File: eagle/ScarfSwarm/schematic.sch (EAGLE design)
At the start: 5 parts

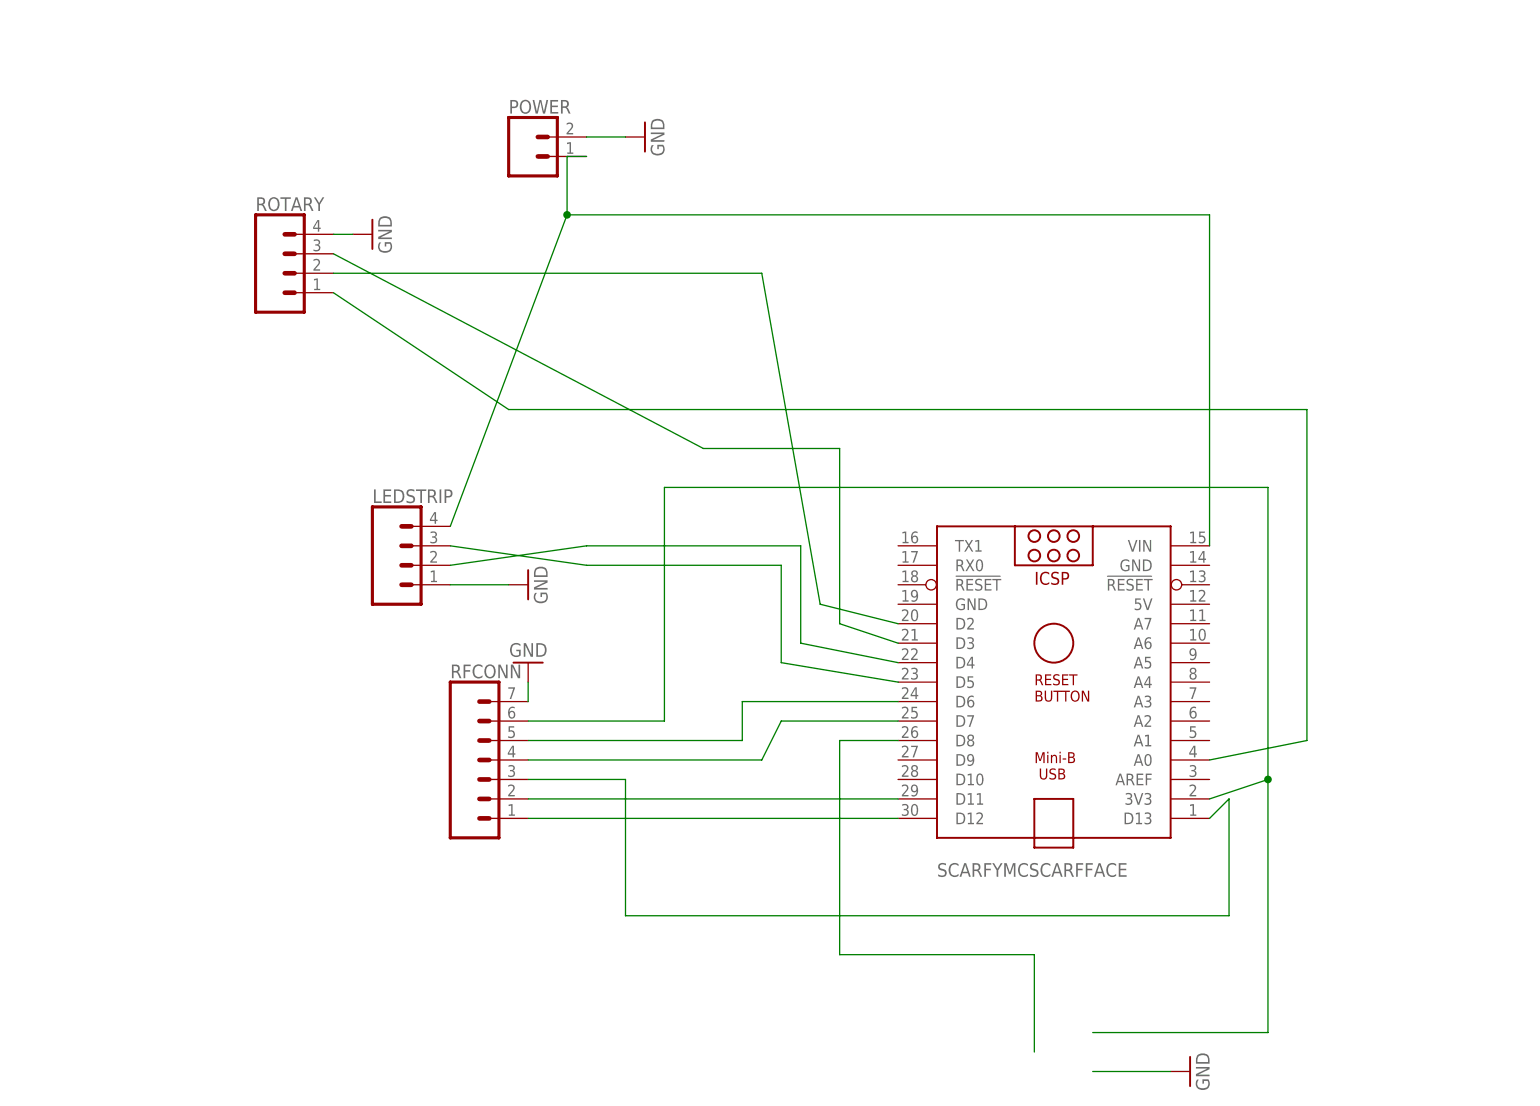
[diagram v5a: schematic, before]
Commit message: reorder radio contacts so that they are easy to solder
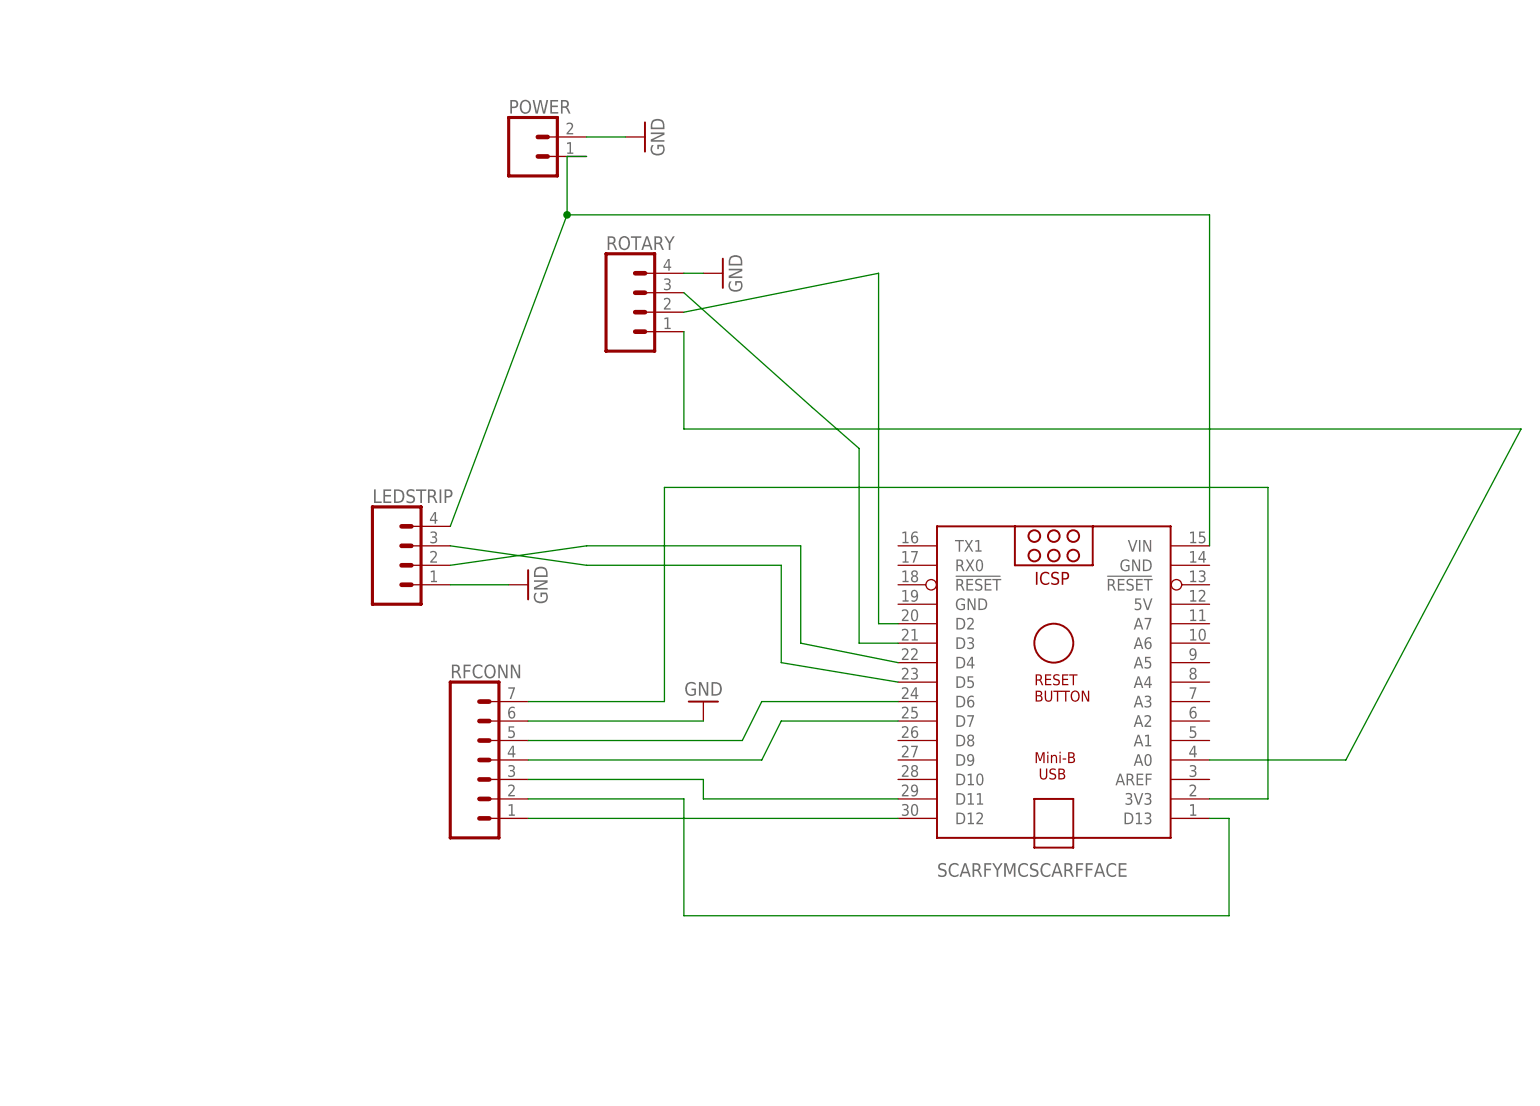
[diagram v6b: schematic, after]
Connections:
- removed net N$7 (its old number): SCARFYMCSCARFFACE.D8
- net GND: now also RFCONN.6; no longer RFCONN.7
- net N$1: now also RFCONN.7; no longer RFCONN.6
- net N$4: now also RFCONN.2; no longer RFCONN.3
- net N$5: now also RFCONN.3; no longer RFCONN.2
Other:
- moved on the sheet: ROTARY
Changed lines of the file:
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@@
 <part name="GND2" library="supply1" library_urn="urn:adsk.eagle:library:371" deviceset="GND" device=""/>
 <part name="SCARFYMCSCARFFACE" library="ArduinoNanoV30" deviceset="ARDUINO_NANO" device=""/>
-<part name="GND5" library="supply1" library_urn="urn:adsk.eagle:library:371" deviceset="GND" device=""/>
 </parts>
 <sheets>
@@
 </plain>
 <instances>
-<instance part="GND1" gate="1" x="-7.62" y="76.2" smashed="yes" rot="R90">
-<attribute name="VALUE" x="-5.08" y="73.66" size="1.778" layer="96" rot="R90"/>
+<instance part="GND1" gate="1" x="38.1" y="71.12" smashed="yes" rot="R90">
+<attribute name="VALUE" x="40.64" y="68.58" size="1.778" layer="96" rot="R90"/>
 </instance>
 <instance part="GND3" gate="1" x="12.7" y="30.48" smashed="yes" rot="R90">
 <attribute name="VALUE" x="15.24" y="27.94" size="1.778" layer="96" rot="R90"/>
 </instance>
-<instance part="GND4" gate="1" x="12.7" y="20.32" smashed="yes" rot="R180">
-<attribute name="VALUE" x="15.24" y="22.86" size="1.778" layer="96" rot="R180"/>
+<instance part="GND4" gate="1" x="35.56" y="15.24" smashed="yes" rot="R180">
+<attribute name="VALUE" x="38.1" y="17.78" size="1.778" layer="96" rot="R180"/>
 </instance>
 <instance part="RFCONN" gate="J1" x="7.62" y="5.08" smashed="yes">
@@
 <attribute name="NAME" x="2.54" y="18.288" size="1.778" layer="95" font="vector"/>
 </instance>
-<instance part="ROTARY" gate="J1" x="-17.78" y="71.12" smashed="yes">
-<attribute name="VALUE" x="-22.86" y="63.754" size="1.778" layer="96" font="vector"/>
-<attribute name="NAME" x="-22.86" y="79.248" size="1.778" layer="95" font="vector"/>
+<instance part="ROTARY" gate="J1" x="27.94" y="66.04" smashed="yes">
+<attribute name="VALUE" x="22.86" y="58.674" size="1.778" layer="96" font="vector"/>
+<attribute name="NAME" x="22.86" y="74.168" size="1.778" layer="95" font="vector"/>
 </instance>
 <instance part="LEDSTRIP" gate="J1" x="-2.54" y="33.02" smashed="yes">
@@
 <attribute name="VALUE" x="66.04" y="-10.16" size="1.778" layer="96"/>
 </instance>
-<instance part="GND5" gate="1" x="99.06" y="-33.02" smashed="yes" rot="R90">
-<attribute name="VALUE" x="101.6" y="-35.56" size="1.778" layer="96" rot="R90"/>
-</instance>
 </instances>
 <busses>
@@
 <nets>
 <net name="GND" class="0">
-<segment>
-<pinref part="RFCONN" gate="J1" pin="7"/>
-<pinref part="GND4" gate="1" pin="GND"/>
-<wire x1="12.7" y1="15.24" x2="12.7" y2="17.78" width="0.1524" layer="91"/>
-</segment>
 <segment>
 <pinref part="LEDSTRIP" gate="J1" pin="1"/>
@@
 <pinref part="ROTARY" gate="J1" pin="4"/>
 <pinref part="GND1" gate="1" pin="GND"/>
-<wire x1="-12.7" y1="76.2" x2="-10.16" y2="76.2" width="0.1524" layer="91"/>
+<wire x1="33.02" y1="71.12" x2="35.56" y2="71.12" width="0.1524" layer="91"/>
 </segment>
 <segment>
@@
 </segment>
 <segment>
-<pinref part="GND5" gate="1" pin="GND"/>
-<wire x1="86.36" y1="-33.02" x2="96.52" y2="-33.02" width="0.1524" layer="91"/>
+<pinref part="RFCONN" gate="J1" pin="6"/>
+<wire x1="12.7" y1="12.7" x2="35.56" y2="12.7" width="0.1524" layer="91"/>
+<pinref part="GND4" gate="1" pin="GND"/>
 </segment>
 </net>
 <net name="N$1" class="0">
 <segment>
-<pinref part="RFCONN" gate="J1" pin="6"/>
-<wire x1="12.7" y1="12.7" x2="30.48" y2="12.7" width="0.1524" layer="91"/>
-<wire x1="30.48" y1="12.7" x2="30.48" y2="43.18" width="0.1524" layer="91"/>
+<wire x1="30.48" y1="15.24" x2="30.48" y2="43.18" width="0.1524" layer="91"/>
 <wire x1="30.48" y1="43.18" x2="109.22" y2="43.18" width="0.1524" layer="91"/>
 <pinref part="SCARFYMCSCARFFACE" gate="G$1" pin="3V3"/>
-<wire x1="109.22" y1="43.18" x2="109.22" y2="5.08" width="0.1524" layer="91"/>
-<wire x1="109.22" y1="5.08" x2="101.6" y2="2.54" width="0.1524" layer="91"/>
-<junction x="109.22" y="5.08"/>
-<wire x1="109.22" y1="5.08" x2="109.22" y2="-27.94" width="0.1524" layer="91"/>
-<wire x1="109.22" y1="-27.94" x2="86.36" y2="-27.94" width="0.1524" layer="91"/>
+<wire x1="109.22" y1="43.18" x2="109.22" y2="2.54" width="0.1524" layer="91"/>
+<wire x1="109.22" y1="2.54" x2="101.6" y2="2.54" width="0.1524" layer="91"/>
+<pinref part="RFCONN" gate="J1" pin="7"/>
+<wire x1="12.7" y1="15.24" x2="30.48" y2="15.24" width="0.1524" layer="91"/>
 </segment>
 </net>
@@
 <pinref part="RFCONN" gate="J1" pin="5"/>
 <wire x1="12.7" y1="10.16" x2="40.64" y2="10.16" width="0.1524" layer="91"/>
-<wire x1="40.64" y1="10.16" x2="40.64" y2="15.24" width="0.1524" layer="91"/>
+<wire x1="40.64" y1="10.16" x2="43.18" y2="15.24" width="0.1524" layer="91"/>
 <pinref part="SCARFYMCSCARFFACE" gate="G$1" pin="D6"/>
-<wire x1="40.64" y1="15.24" x2="60.96" y2="15.24" width="0.1524" layer="91"/>
+<wire x1="43.18" y1="15.24" x2="60.96" y2="15.24" width="0.1524" layer="91"/>
 </segment>
 </net>
@@
 <net name="N$4" class="0">
 <segment>
-<pinref part="RFCONN" gate="J1" pin="3"/>
-<wire x1="12.7" y1="5.08" x2="25.4" y2="5.08" width="0.1524" layer="91"/>
-<wire x1="25.4" y1="5.08" x2="25.4" y2="-12.7" width="0.1524" layer="91"/>
-<wire x1="25.4" y1="-12.7" x2="104.14" y2="-12.7" width="0.1524" layer="91"/>
 <pinref part="SCARFYMCSCARFFACE" gate="G$1" pin="D13"/>
-<wire x1="104.14" y1="-12.7" x2="104.14" y2="2.54" width="0.1524" layer="91"/>
-<wire x1="104.14" y1="2.54" x2="101.6" y2="0" width="0.1524" layer="91"/>
-</segment>
-</net>
-<net name="N$5" class="0">
-<segment>
+<wire x1="33.02" y1="-12.7" x2="104.14" y2="-12.7" width="0.1524" layer="91"/>
+<wire x1="104.14" y1="-12.7" x2="104.14" y2="0" width="0.1524" layer="91"/>
+<wire x1="104.14" y1="0" x2="101.6" y2="0" width="0.1524" layer="91"/>
 <pinref part="RFCONN" gate="J1" pin="2"/>
-<wire x1="12.7" y1="2.54" x2="60.96" y2="2.54" width="0.1524" layer="91"/>
-<pinref part="SCARFYMCSCARFFACE" gate="G$1" pin="D11"/>
-</segment>
-</net>
-<net name="N$6" class="0">
-<segment>
-<pinref part="RFCONN" gate="J1" pin="1"/>
-<wire x1="60.96" y1="0" x2="12.7" y2="0" width="0.1524" layer="91"/>
-<pinref part="SCARFYMCSCARFFACE" gate="G$1" pin="D12"/>
+<wire x1="12.7" y1="2.54" x2="33.02" y2="2.54" width="0.1524" layer="91"/>
+<wire x1="33.02" y1="2.54" x2="33.02" y2="-12.7" width="0.1524" layer="91"/>
 </segment>
 </net>
@@
 <segment>
 <pinref part="ROTARY" gate="J1" pin="3"/>
-<wire x1="-12.7" y1="73.66" x2="35.56" y2="48.26" width="0.1524" layer="91"/>
-<wire x1="35.56" y1="48.26" x2="53.34" y2="48.26" width="0.1524" layer="91"/>
+<wire x1="33.02" y1="68.58" x2="49.784" y2="53.594" width="0.1524" layer="91"/>
+<wire x1="49.784" y1="53.594" x2="55.88" y2="48.26" width="0.1524" layer="91"/>
 <pinref part="SCARFYMCSCARFFACE" gate="G$1" pin="D3"/>
-<wire x1="53.34" y1="48.26" x2="53.34" y2="25.4" width="0.1524" layer="91"/>
-<wire x1="53.34" y1="25.4" x2="60.96" y2="22.86" width="0.1524" layer="91"/>
+<wire x1="55.88" y1="48.26" x2="55.88" y2="22.86" width="0.1524" layer="91"/>
+<wire x1="55.88" y1="22.86" x2="60.96" y2="22.86" width="0.1524" layer="91"/>
 </segment>
 </net>
@@
 <segment>
 <pinref part="ROTARY" gate="J1" pin="2"/>
-<wire x1="-12.7" y1="71.12" x2="43.18" y2="71.12" width="0.1524" layer="91"/>
-<wire x1="43.18" y1="71.12" x2="50.8" y2="27.94" width="0.1524" layer="91"/>
+<wire x1="33.02" y1="66.04" x2="58.42" y2="71.12" width="0.1524" layer="91"/>
+<wire x1="58.42" y1="71.12" x2="58.42" y2="25.4" width="0.1524" layer="91"/>
 <pinref part="SCARFYMCSCARFFACE" gate="G$1" pin="D2"/>
-<wire x1="50.8" y1="27.94" x2="60.96" y2="25.4" width="0.1524" layer="91"/>
+<wire x1="58.42" y1="25.4" x2="60.96" y2="25.4" width="0.1524" layer="91"/>
 </segment>
 </net>
@@
 <segment>
 <pinref part="ROTARY" gate="J1" pin="1"/>
-<wire x1="-12.7" y1="68.58" x2="10.16" y2="53.34" width="0.1524" layer="91"/>
-<wire x1="10.16" y1="53.34" x2="114.3" y2="53.34" width="0.1524" layer="91"/>
-<wire x1="114.3" y1="53.34" x2="114.3" y2="10.16" width="0.1524" layer="91"/>
+<wire x1="33.02" y1="63.5" x2="33.02" y2="50.8" width="0.1524" layer="91"/>
+<wire x1="33.02" y1="50.8" x2="142.24" y2="50.8" width="0.1524" layer="91"/>
+<wire x1="142.24" y1="50.8" x2="119.38" y2="7.62" width="0.1524" layer="91"/>
 <pinref part="SCARFYMCSCARFFACE" gate="G$1" pin="A0"/>
-<wire x1="114.3" y1="10.16" x2="101.6" y2="7.62" width="0.1524" layer="91"/>
+<wire x1="119.38" y1="7.62" x2="101.6" y2="7.62" width="0.1524" layer="91"/>
 </segment>
 </net>
@@
 </segment>
 </net>
+<net name="N$5" class="0">
+<segment>
+<pinref part="RFCONN" gate="J1" pin="3"/>
+<wire x1="12.7" y1="5.08" x2="35.56" y2="5.08" width="0.1524" layer="91"/>
+<wire x1="35.56" y1="5.08" x2="35.56" y2="2.54" width="0.1524" layer="91"/>
+<pinref part="SCARFYMCSCARFFACE" gate="G$1" pin="D11"/>
+<wire x1="35.56" y1="2.54" x2="60.96" y2="2.54" width="0.1524" layer="91"/>
+</segment>
+</net>
 <net name="N$7" class="0">
 <segment>
-<pinref part="SCARFYMCSCARFFACE" gate="G$1" pin="D8"/>
-<wire x1="60.96" y1="10.16" x2="53.34" y2="10.16" width="0.1524" layer="91"/>
-<wire x1="53.34" y1="10.16" x2="53.34" y2="-17.78" width="0.1524" layer="91"/>
-<wire x1="53.34" y1="-17.78" x2="78.74" y2="-17.78" width="0.1524" layer="91"/>
-<wire x1="78.74" y1="-17.78" x2="78.74" y2="-30.48" width="0.1524" layer="91"/>
+<pinref part="RFCONN" gate="J1" pin="1"/>
+<pinref part="SCARFYMCSCARFFACE" gate="G$1" pin="D12"/>
+<wire x1="12.7" y1="0" x2="60.96" y2="0" width="0.1524" layer="91"/>
 </segment>
 </net>
